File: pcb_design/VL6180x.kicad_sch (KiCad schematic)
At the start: 6 parts, among them J17 ToF, U4 VL6180XV0NR/1

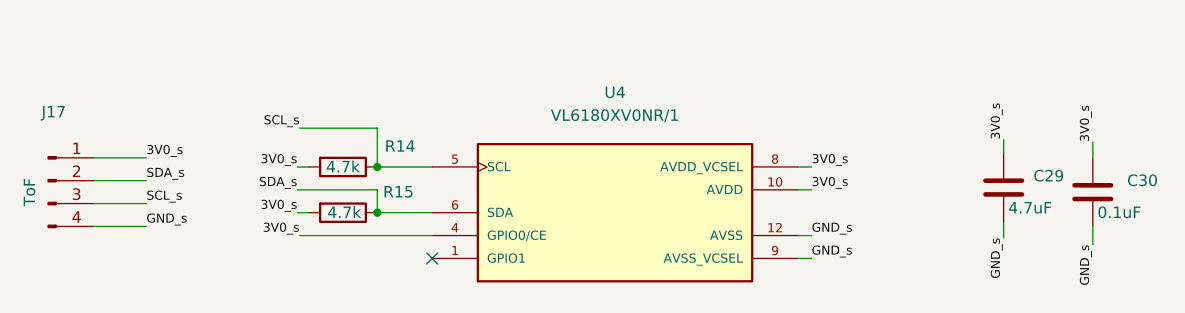
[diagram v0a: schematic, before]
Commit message: Update Mushak PCB design to include new features (#5)
* Update mushak PCB with new changes
* Add AMS1117 as 3.3v regulator
* Add new alternate placement for IR sensors
* Add new 3.3v compatible ToF sensor
* Update gerber files

* Add changes to silkscreen and filter capacitors
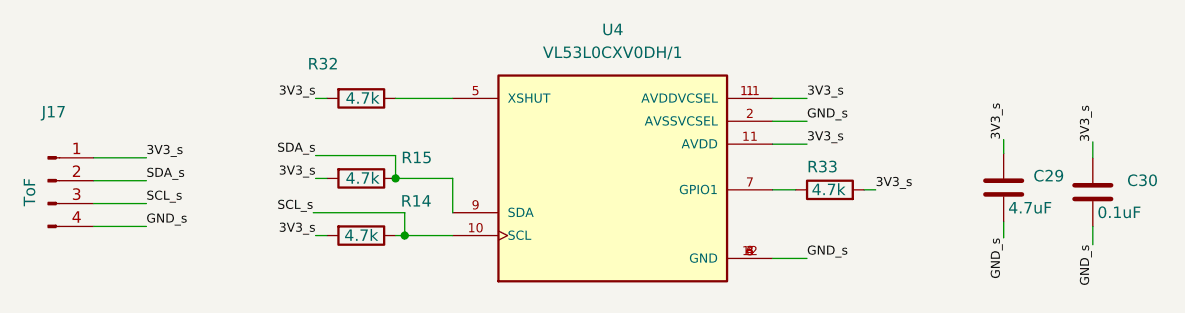
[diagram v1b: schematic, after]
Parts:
- removed U4: VL6180XV0NR/1, VL6180XV0NR_1:LGA12R75P2X6_280X480X110, symbol VL6180XV0NR_1:VL6180XV0NR/1
- added R32, R33: 4.7k, Resistor_SMD:R_0402_1005Metric, symbol Device:R
- added U4: VL53L0CXV0DH/1, VL53L0CXV0DH_1:XDCR_VL53L0CXV0DH_1, symbol VL53L0CXV0DH_1:VL53L0CXV0DH/1
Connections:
- net GND_s: now also U4.12 (GND), U4.2 (AVSSVCSEL), U4.3 (GND), U4.4 (GND), U4.6 (GND)
- net SCL_s: now also U4.10 (SCL)
- net SDA_s: now also U4.9 (SDA)
- net 3V0_s renamed 3V3_s
- net 3V3_s: now also R32.2, R33.2, U4.1 (AVDDVCSEL), U4.1.1 (AVDDVCSEL), U4.11 (AVDD)
- new net: R32.1, U4.5 (XSHUT)
- new net: R33.1, U4.7 (GPIO1)
- no-connect marks 1 -> 0
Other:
- moved on the sheet: R14, R15
